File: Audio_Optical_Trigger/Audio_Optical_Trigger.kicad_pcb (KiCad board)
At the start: 2 copper layers, 115 parts, among them J1001 Trigger Output, J201 +12VIN, J301 TX1, J302 RX1, J401 TX2, J402 RX2, J501 TX3, J502 RX3, J901 Group Select, U201 74LVC1G14, U202 TPS62130, U301 74LVC1G17, U401 74LVC1G17, U501 74LVC1G17, U601 74LVC1G38, U602 74LVC1G38, U603 74LVC1G38, U701 74LVC1G38, U702 74LVC1G38, U703 74LVC1G38, U801 74LVC1G38, U802 74LVC1G38, U803 74LVC1G38, U901 74LVC1G14, U902 74LVC1G14, U903 74LVC1G14

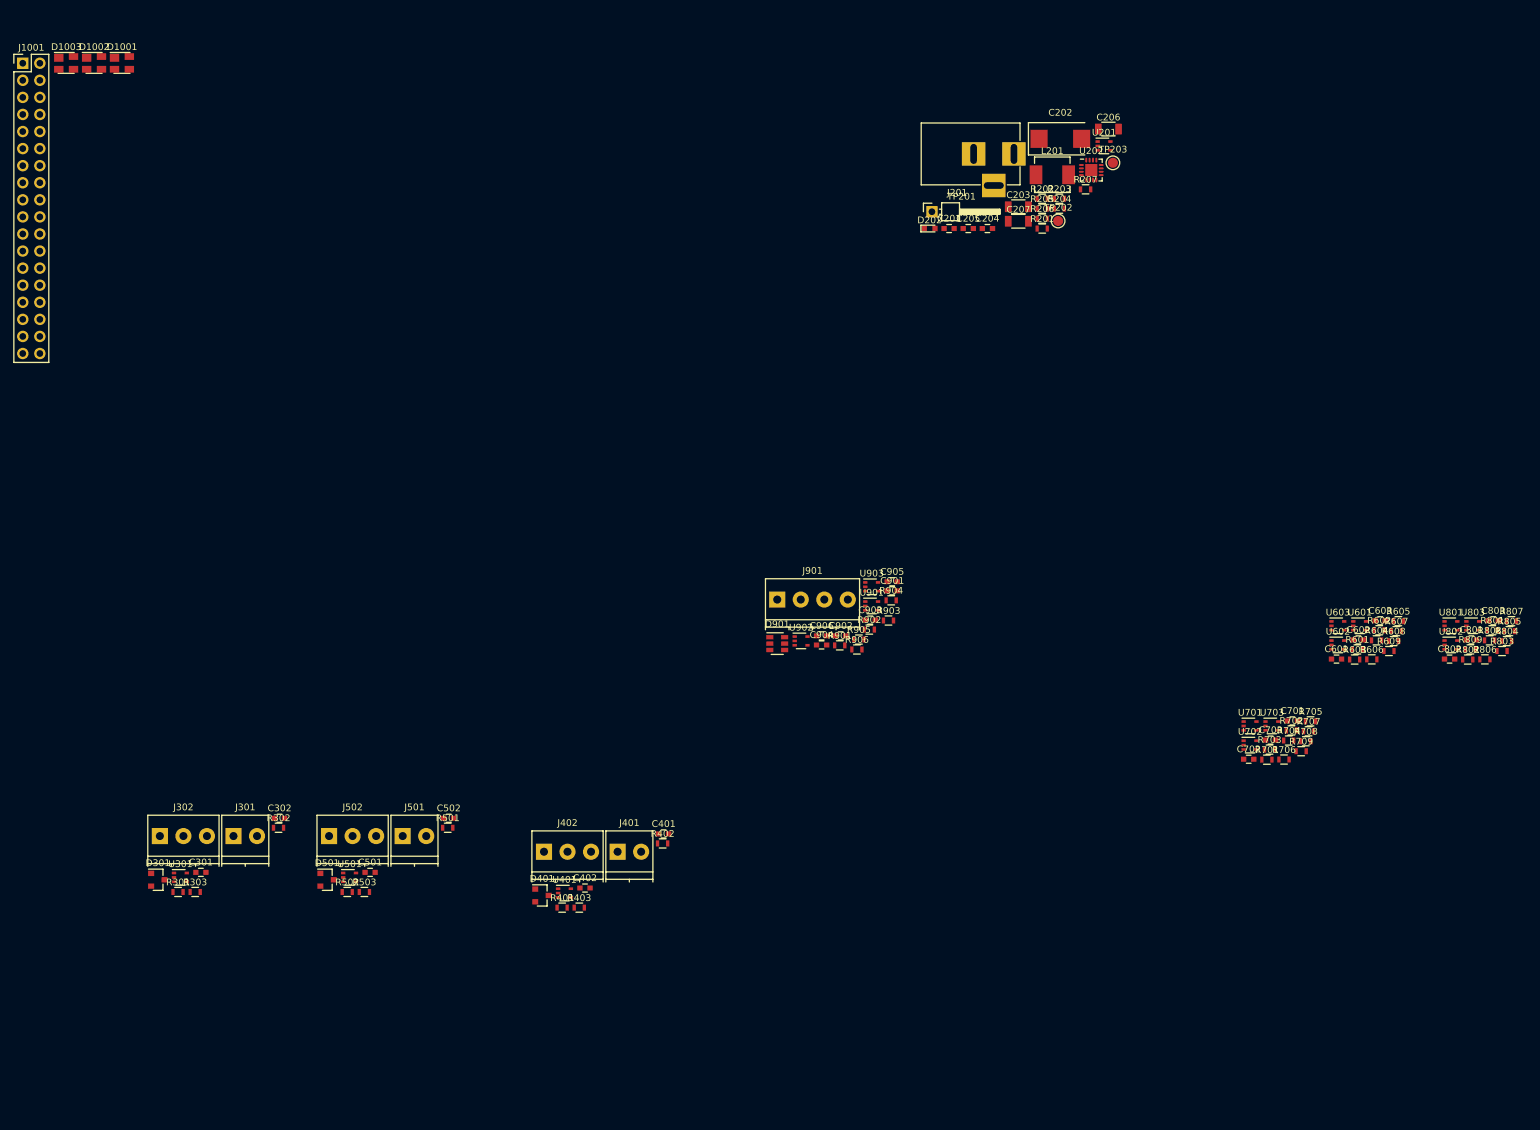
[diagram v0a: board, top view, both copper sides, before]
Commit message: Fixed diode footprint issue
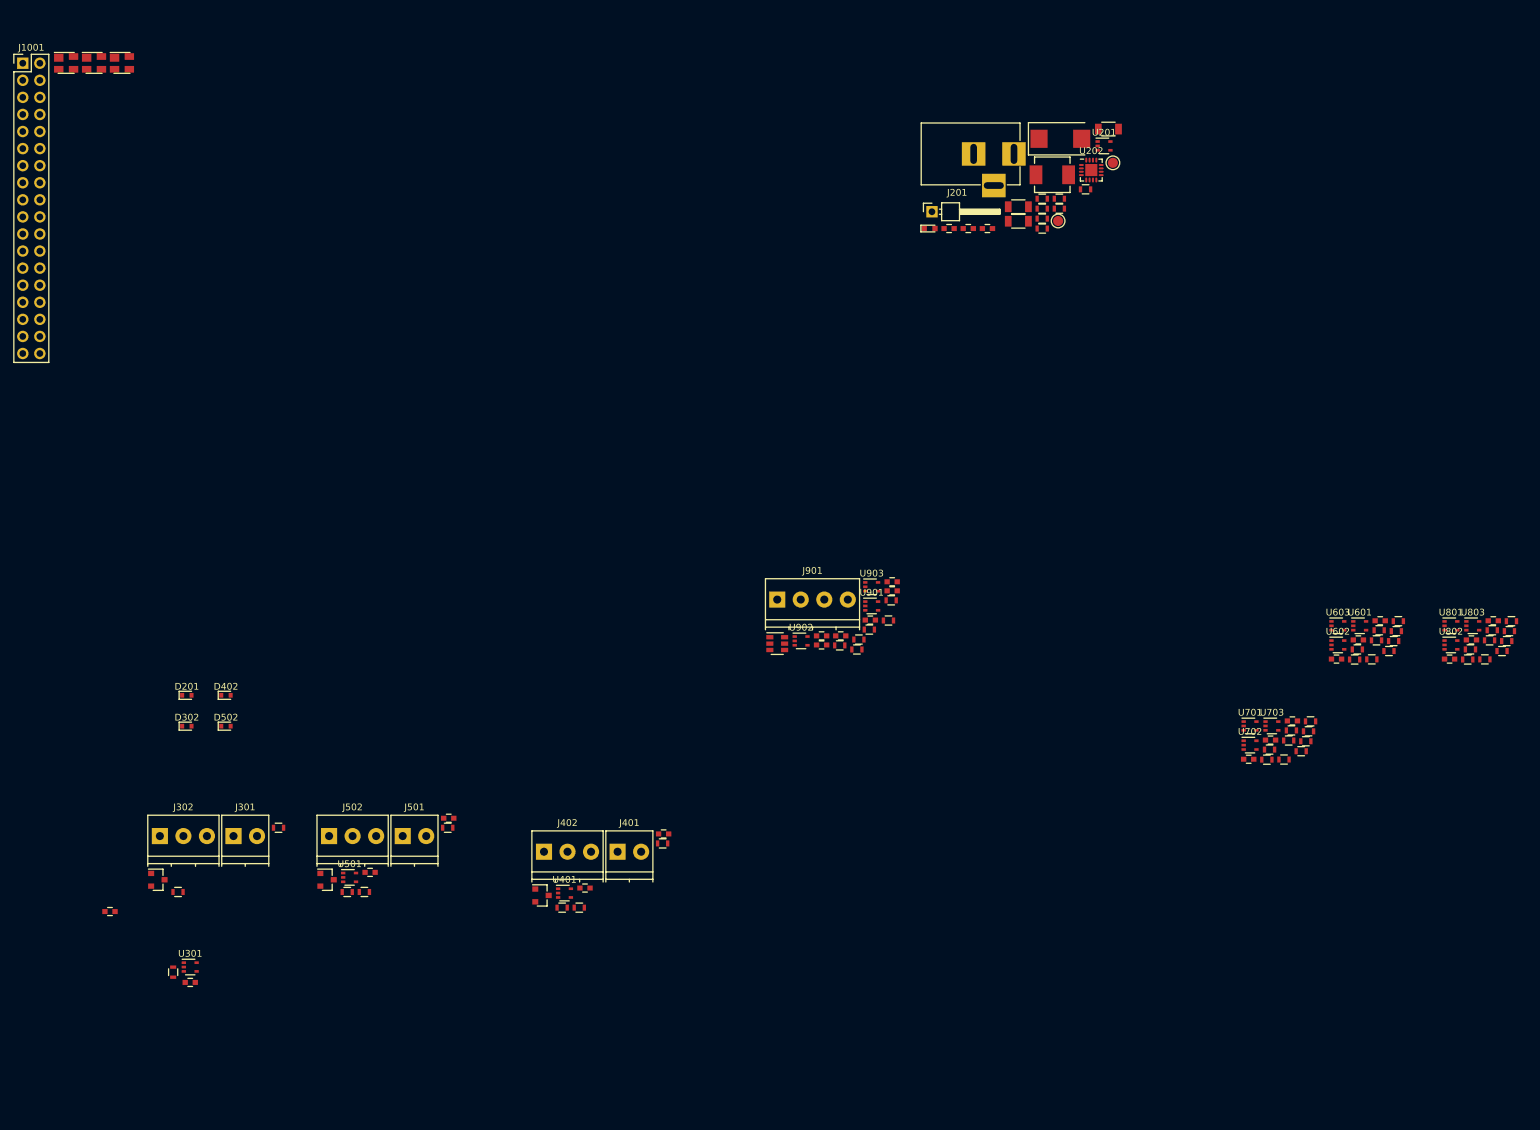
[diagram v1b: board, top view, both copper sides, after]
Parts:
- added D201: MM5Z10V, Diodes_SMD:D_SOD-523, F.Cu at (48.4, 110.7)
- added D302: MM5Z5V6, Diodes_SMD:D_SOD-523, F.Cu at (48.4, 115.3)
- added D402: MM5Z5V6, Diodes_SMD:D_SOD-523, F.Cu at (54.2, 110.7)
- added D502: MM5Z5V6, Diodes_SMD:D_SOD-523, F.Cu at (54.2, 115.3)
- moved C302 27.8 mm to (48.9, 153.4), turned to 180 degrees
- moved C301 14.7 mm to (37.0, 142.9)
- moved U301 13.4 mm to (48.9, 151.1)
- moved R303 12.4 mm to (46.4, 151.9), turned to 90 degrees
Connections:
- R201 pad 1: (no net) -> Net-(D201-Pad2)

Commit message: Rewired a few nets, placed some parts
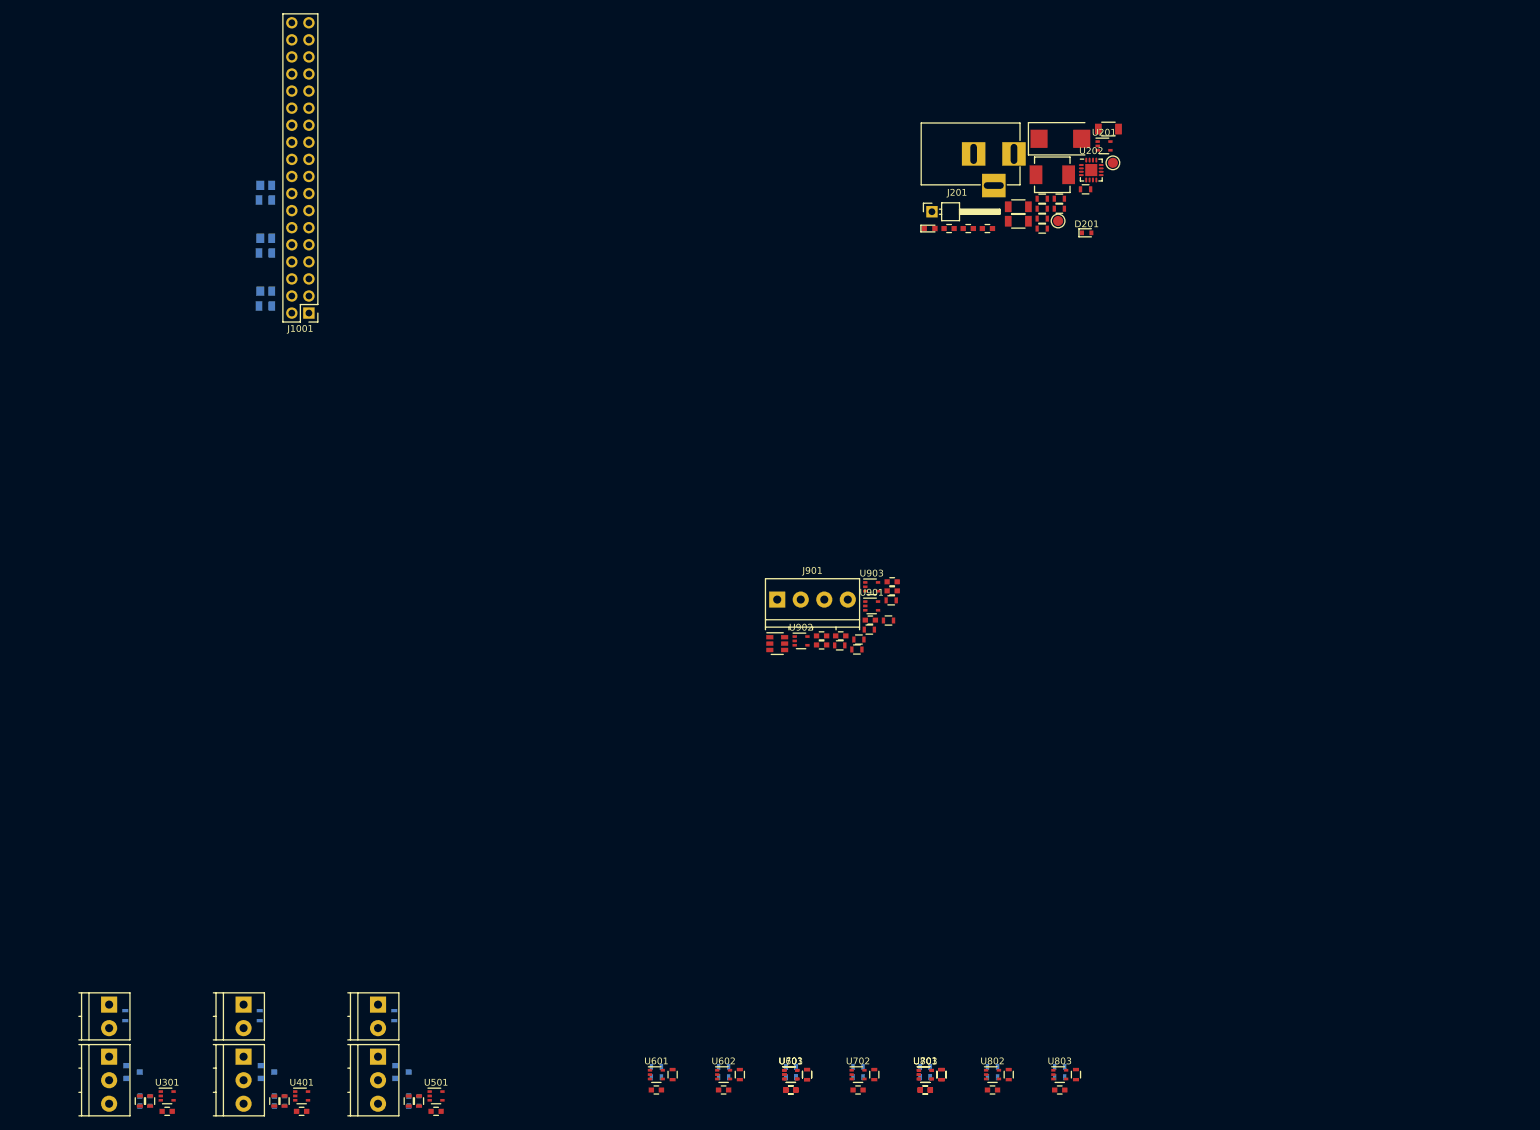
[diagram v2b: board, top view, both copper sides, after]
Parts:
- C301, C401, C501, D1001, D1002, D1003, D301, D302, D401, D402, D501, D502, R301, R401, R501, R601, R602, R603, R604, R605, R606: moved to B.Cu
- moved D201 150.5 mm to (182.2, 41.9)
- moved R607 126.3 mm to (120.7, 167.1), turned to 270 degrees
- moved R604 125.3 mm to (118.2, 167.5)
- moved U601 124.1 mm to (118.2, 167.1)
- moved R601 121.4 mm to (118.2, 166.0)
- moved R605 121.1 mm to (128.2, 167.5)
- moved C601 119.8 mm to (118.2, 169.4), turned to 180 degrees
- moved R602 117.2 mm to (128.2, 166.0)
- moved R608 116.7 mm to (130.7, 167.1), turned to 270 degrees
- moved C602 115.7 mm to (128.2, 169.4), turned to 180 degrees
- moved C603 112.1 mm to (138.2, 169.4), turned to 180 degrees
- moved U602 111.5 mm to (128.2, 167.1)
- moved R807 108.3 mm to (160.7, 167.1), turned to 270 degrees
- moved R804 108.1 mm to (158.2, 167.5)
- moved R609 107.1 mm to (140.7, 167.1), turned to 270 degrees
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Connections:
- D1001 pad 2: ~Output_Group_1_Channel_1 -> ~Output_Group_1_Channel_3
- D1001 pad 4: ~Output_Group_1_Channel_3 -> ~Output_Group_1_Channel_1
- D1002 pad 2: ~Output_Group_2_Channel_1 -> ~Output_Group_2_Channel_3
- D1002 pad 4: ~Output_Group_2_Channel_3 -> ~Output_Group_2_Channel_1
- D1003 pad 2: ~Output_Group_3_Channel_1 -> ~Output_Group_3_Channel_3
- D1003 pad 4: ~Output_Group_3_Channel_3 -> ~Output_Group_3_Channel_1

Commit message: Determined PCB shape
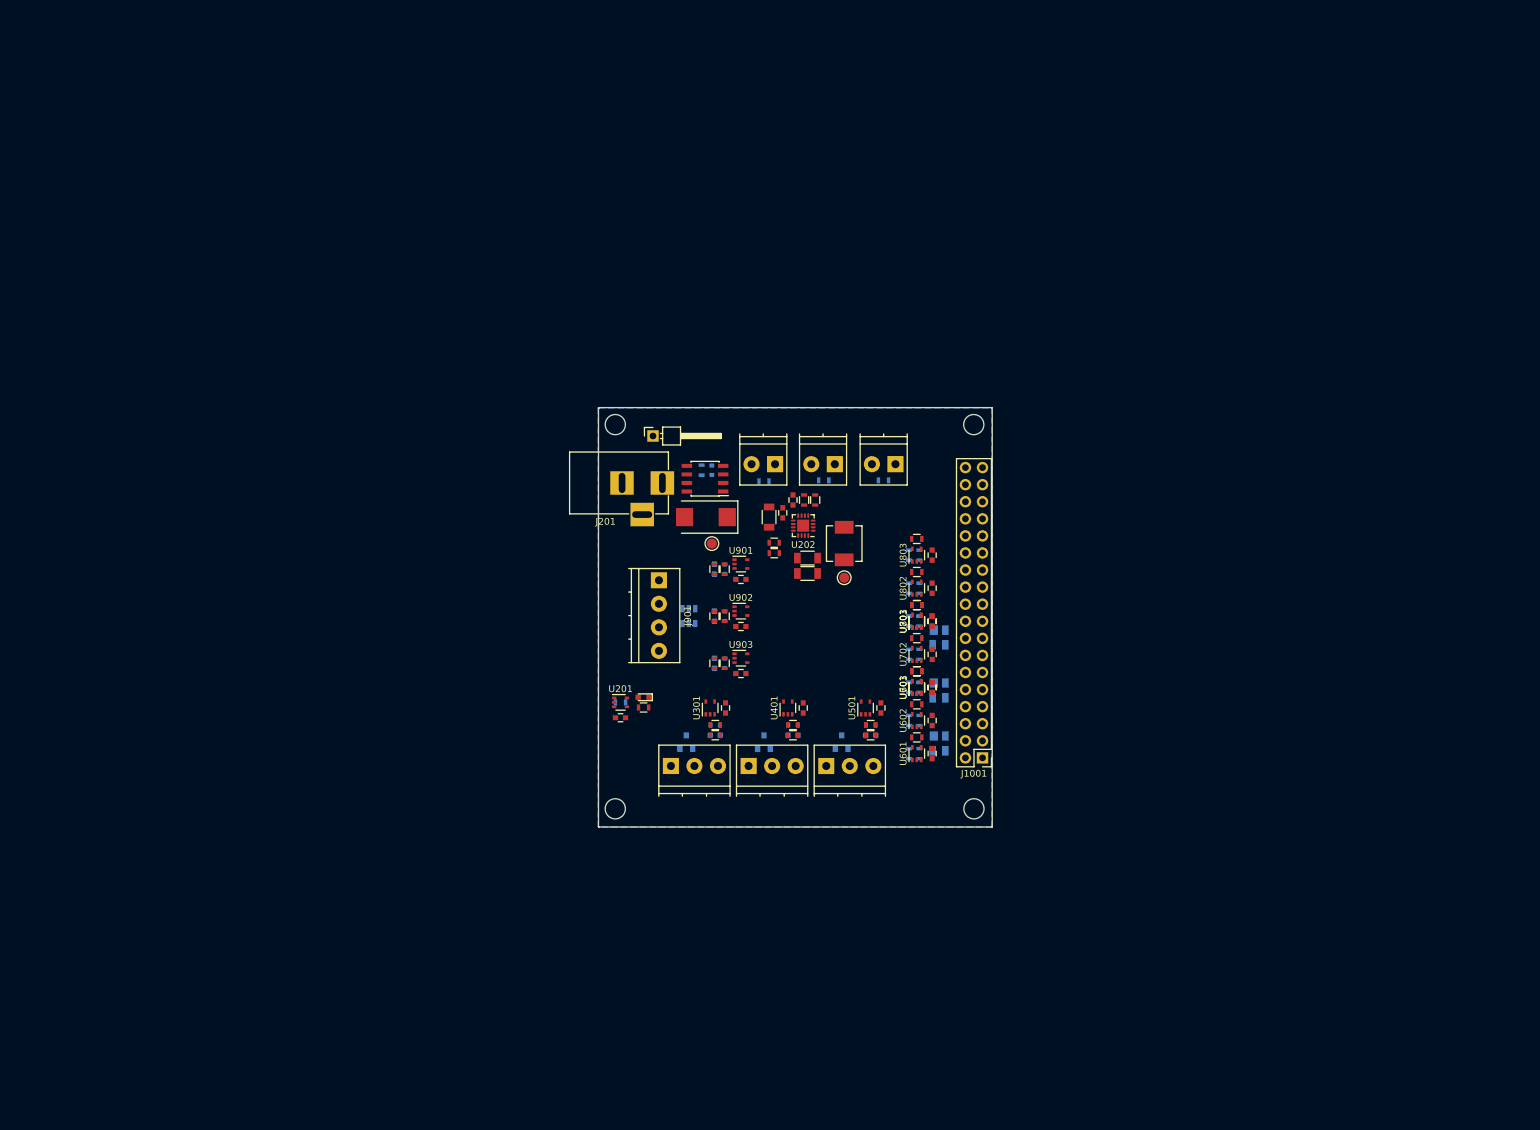
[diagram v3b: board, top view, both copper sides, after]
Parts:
- removed the C904 at (142.8, 103.2)
- added C905: 0.1uF, Capacitors_SMD:C_0603, F.Cu at (130.8, 100.5)
- added D902: MM5Z5V6, Diodes_SMD:D_SOD-523, B.Cu at (128.4, 91.9)
- added D903: MM5Z5V6, Diodes_SMD:D_SOD-523, B.Cu at (128.4, 98.9)
- added D904: MM5Z5V6, Diodes_SMD:D_SOD-523, B.Cu at (128.4, 105.9)
- added H1101: MountingHole, Mounting_Holes:MountingHole_3mm, B.Cu at (165.4, 70.4)
- added H1102: MountingHole, Mounting_Holes:MountingHole_3mm, B.Cu at (112.1, 70.4)
- added H1103: MountingHole, Mounting_Holes:MountingHole_3mm, B.Cu at (165.5, 127.6)
- added H1104: MountingHole, Mounting_Holes:MountingHole_3mm, B.Cu at (112.1, 127.6)
- added Q201: IRF7404, Housings_SOIC:SOIC-8_3.9x4.9mm_Pitch1.27mm, F.Cu at (125.5, 78.5)
- C901, C902, C903, D201, D901, R201, R203: moved to B.Cu
- moved J301 127.6 mm to (135.9, 76.3), turned to 180 degrees
- moved R301 123.9 mm to (134.2, 78.9), turned to 0 degrees
- moved D1001 120.1 mm to (160.3, 117.9)
- moved D1002 120.1 mm to (160.3, 110.0)
- moved D1003 120.1 mm to (160.3, 102.1)
- moved J1001 120.1 mm to (166.8, 120.0)
- moved J401 119.2 mm to (144.8, 76.3), turned to 180 degrees
- moved R401 115.7 mm to (143.1, 78.7), turned to 0 degrees
- moved J501 111.3 mm to (153.8, 76.3), turned to 180 degrees
- moved U201 109.7 mm to (112.9, 111.8)
- moved R501 107.9 mm to (152.0, 78.7), turned to 0 degrees
- moved C302 102.5 mm to (128.5, 112.6), turned to 270 degrees
- moved C301 101.4 mm to (127.0, 116.6), turned to 0 degrees
- moved R302 101.4 mm to (127.0, 116.6), turned to 0 degrees
- moved D302 101.0 mm to (127.0, 115.1), turned to 0 degrees
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- renumbered C905 to C904
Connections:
- J201 pad 1: (no net) -> Net-(J201-Pad1)
- J901 pad 1: Net-(D901-Pad1) -> Net-(D901-Pad3)
- J901 pad 2: Net-(D901-Pad3) -> Net-(D901-Pad1)
- R606 pad 1: Input_Channel_2 -> Input_Channel_3
- R706 pad 1: Input_Channel_2 -> Input_Channel_3
- R806 pad 1: Input_Channel_2 -> Input_Channel_3
- R901 pad 2: Net-(D901-Pad1) -> Net-(D901-Pad3)
- R902 pad 2: Net-(D901-Pad3) -> Net-(D901-Pad1)
- U501 pad 4: (no net) -> Input_Channel_3
- U603 pad 2: Input_Channel_2 -> Input_Channel_3
- U703 pad 2: Input_Channel_2 -> Input_Channel_3
- U803 pad 2: Input_Channel_2 -> Input_Channel_3
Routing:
- added copper zone on B.Cu, net GND
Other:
- board outline added: 58.6 x 62.4 mm
- net class Power added: clearance 0.127, trace_width 0.635, via_dia 0.8, via_drill 0.4
- net class Signal added: clearance 0.127, trace_width 0.254, via_dia 0.8, via_drill 0.4

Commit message: Routed board in one go
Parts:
- R701, R702, R703, R704, R705, R706, R801, R802, R803, R804, R805, R806: moved to B.Cu
- moved R803 8.67 mm to (157.1, 81.3), turned to 0 degrees
- moved R802 8.52 mm to (157.1, 86.4), turned to 0 degrees
- moved R801 8.36 mm to (157.1, 91.4), turned to 0 degrees
- moved U803 7.57 mm to (157.4, 82.3), turned to 0 degrees
- moved U802 7.41 mm to (157.4, 87.4), turned to 0 degrees
- moved U801 7.25 mm to (157.4, 92.5), turned to 0 degrees
- moved R806 7.06 mm to (157.1, 82.8), turned to 0 degrees
- moved R805 6.90 mm to (157.1, 87.9), turned to 0 degrees
- moved R607 6.76 mm to (159.9, 123.1), turned to 270 degrees
- moved R804 6.74 mm to (157.1, 93.0), turned to 0 degrees
- moved R608 6.62 mm to (159.9, 118.0), turned to 270 degrees
- moved R609 6.47 mm to (159.9, 112.9), turned to 270 degrees
- moved C601 6.14 mm to (157.4, 125.2), turned to 180 degrees
- moved C602 5.99 mm to (157.4, 120.1), turned to 180 degrees
- moved C603 5.84 mm to (157.4, 115.1), turned to 180 degrees
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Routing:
- net Input_Channel_1: track 0.00 -> 75.3 mm, vias 0 -> 6
- net Output_Group_Select_3: track 0.00 -> 66.6 mm, vias 0 -> 7
- net Input_Channel_2: track 0.00 -> 63.4 mm, vias 0 -> 7
- net Output_Group_Select_1: track 0.00 -> 61.1 mm, vias 0 -> 7
- net POS5_PGOOD: track 0.00 -> 54.7 mm, vias 0 -> 3
- net Output_Group_Select_2: track 0.00 -> 53.9 mm, vias 0 -> 7
- net Input_Channel_3: track 0.00 -> 53.4 mm, vias 0 -> 7
- net GND: track 0.00 -> 52.8 mm, vias 0 -> 72
- net ~Output_Group_3_Channel_3: track 0.00 -> 30.9 mm
- net ~Output_Group_3_Channel_1: track 0.00 -> 29.9 mm
- net ~Output_Group_3_Channel_2: track 0.00 -> 28.6 mm
- net ~Output_Group_2_Channel_3: track 0.00 -> 23.6 mm
- net ~Output_Group_1_Channel_1: track 0.00 -> 22.2 mm
- net ~Output_Group_2_Channel_1: track 0.00 -> 22.0 mm
- net ~Output_Group_2_Channel_2: track 0.00 -> 20.9 mm
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- added copper zone on F.Cu, net +12V
- added copper zone on F.Cu, net +5V
- added copper zone on F.Cu, net GND
- added copper zone on F.Cu, net Net-(J201-Pad1)
- added copper zone on F.Cu, net Net-(L201-Pad1)
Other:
- net class Default: clearance 0.2 -> 0.127; trace_width 0.25 -> 0.254; via_dia 0.8 -> 0.508; via_drill 0.4 -> 0.254
- net class Power: via_dia 0.8 -> 0.508; via_drill 0.4 -> 0.254
- net class Signal: via_dia 0.8 -> 0.508; via_drill 0.4 -> 0.254
- rule trace_clearance: 0.2 -> 0.127
- rule trace_min: 0.2 -> 0.127
- rule via_min_drill: 0.3 -> 0.254
- rule via_min_size: 0.4 -> 0.508
